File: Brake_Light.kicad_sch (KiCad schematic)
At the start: 3 parts, among them IC1 ADP1610ARMZ-R7, J1 Conn_01x06, J2 Conn_01x02

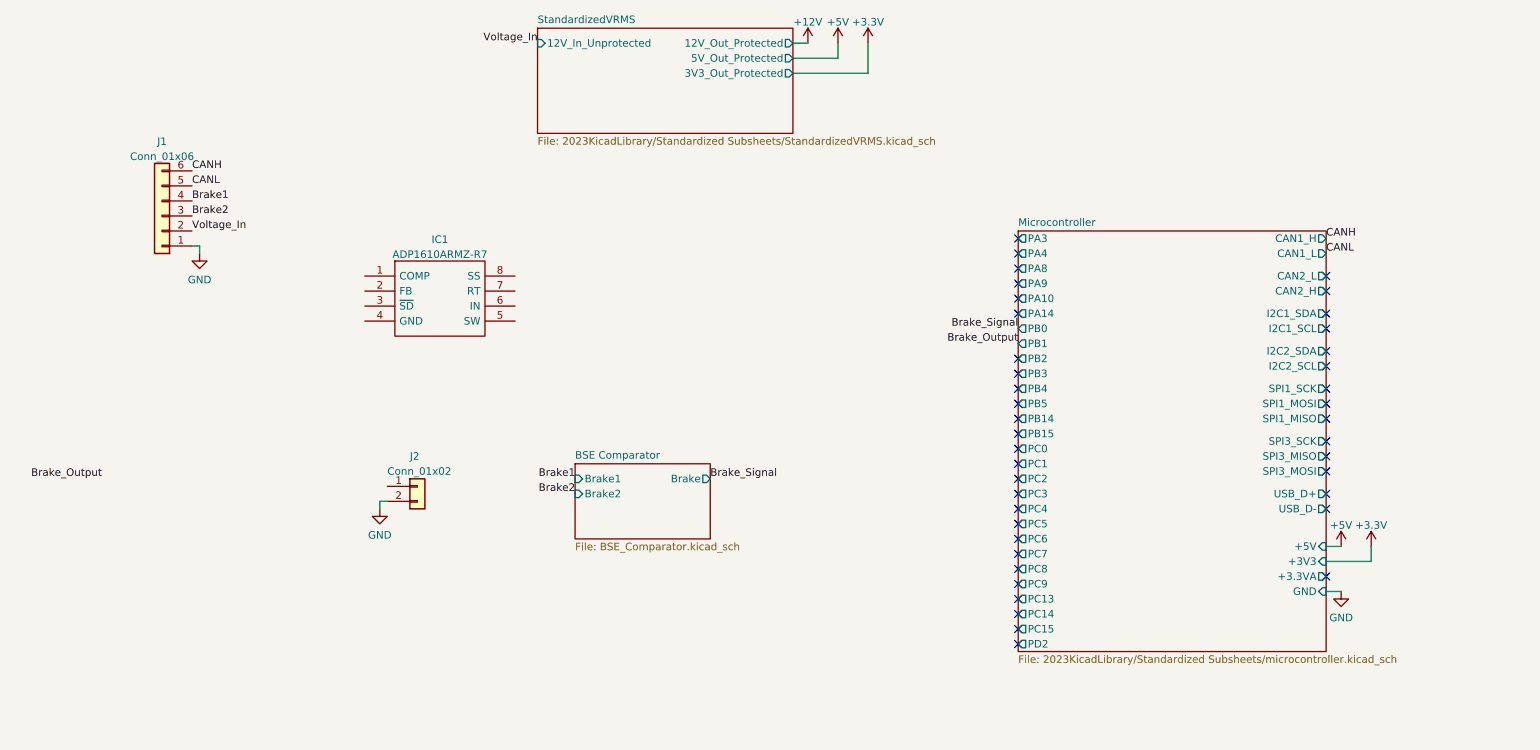
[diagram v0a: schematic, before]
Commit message: completed initial schematic
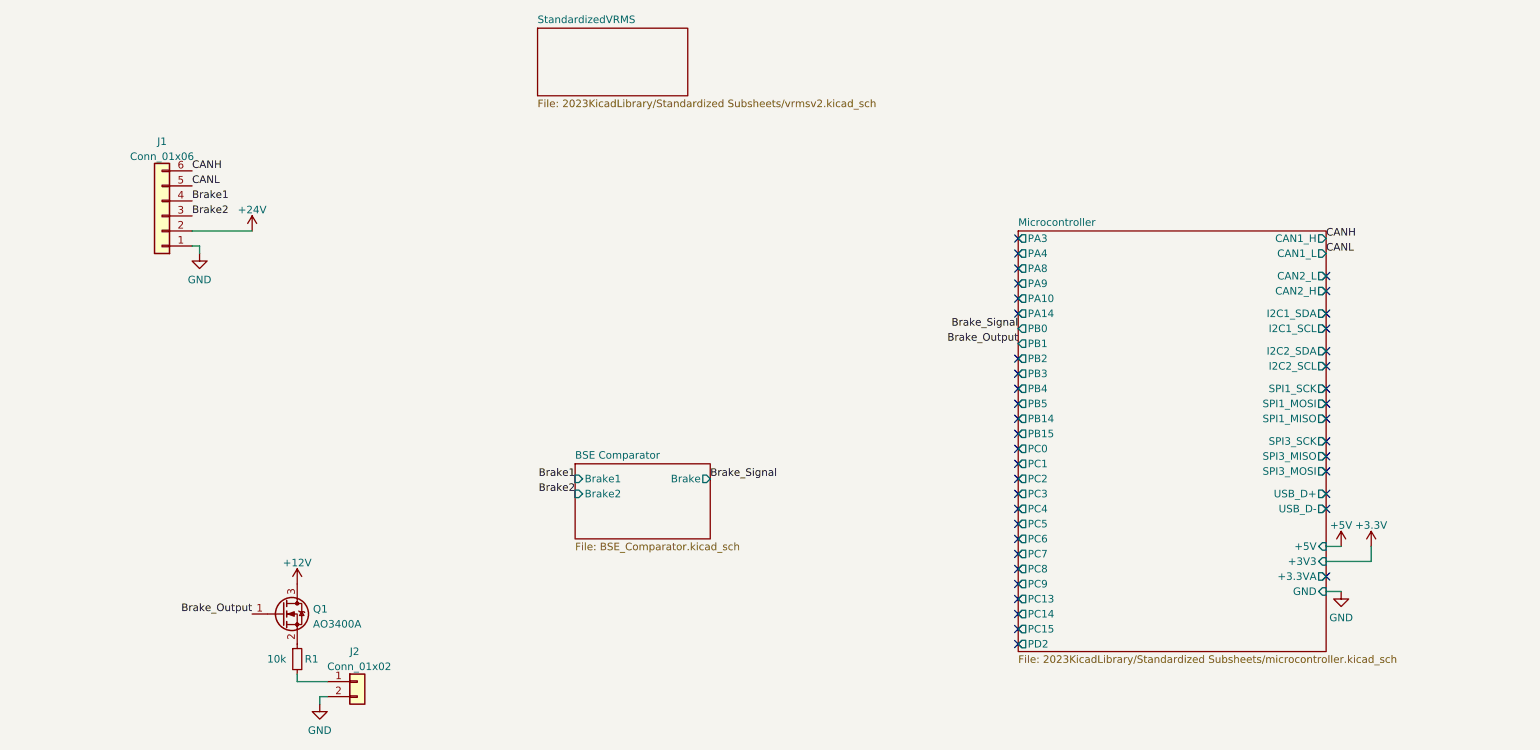
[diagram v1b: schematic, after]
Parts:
- removed IC1: ADP1610ARMZ-R7, Global Libraries:SOP65P490X110-8N, symbol Global_Library:ADP1610ARMZ-R7
- added Q1: AO3400A, Package_TO_SOT_SMD:SOT-23, symbol Transistor_FET:AO3400A
- added R1: 10k, symbol Device:R_Small
- J1: footprint (none) -> Connector_PinHeader_2.54mm:PinHeader_1x06_P2.54mm_Vertical
- J2: footprint (none) -> Connector_PinHeader_2.54mm:PinHeader_1x02_P2.54mm_Vertical
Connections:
- net +12V: now also Q1.3 (D)
- net Brake_Output: now also Q1.1 (G)
- net at J2.1 (Pin_1): now also R1.2
- net Voltage_In renamed +24V
- new net: Q1.2 (S), R1.1
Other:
- sheet StandardizedVRMS: file 2023KicadLibrary/Standardized Subsheets/StandardizedVRMS.kicad_sch -> 2023KicadLibrary/Standardized Subsheets/vrmsv2.kicad_sch
- sheet StandardizedVRMS ports: added none; removed 12V_In_Unprotected, 12V_Out_Protected, 3V3_Out_Protected, 5V_Out_Protected
- moved on the sheet: J2
